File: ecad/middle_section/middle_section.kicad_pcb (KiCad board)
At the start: 2 copper layers, 100 x 80 mm, 28 parts, among them J1 JST SH, J2 JST SH, J5 Conn_01x08, U1 ATtiny1617-M

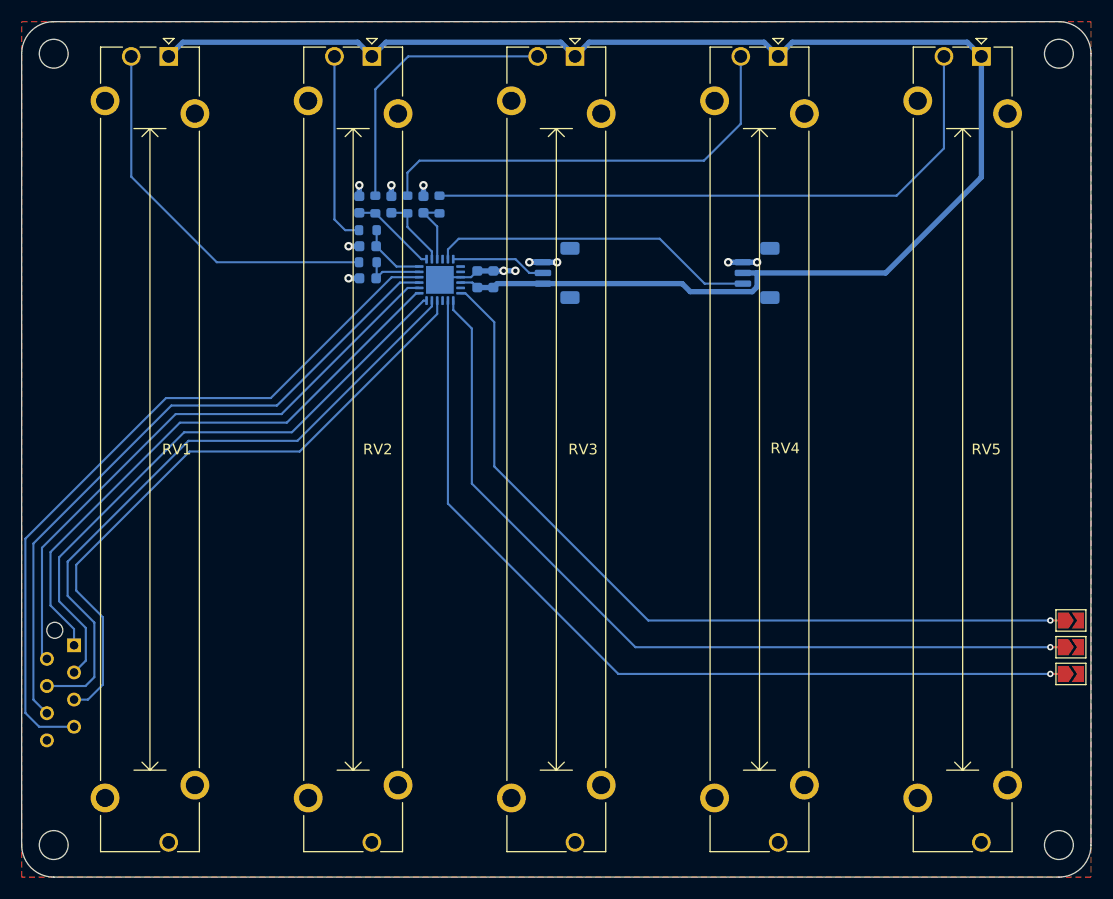
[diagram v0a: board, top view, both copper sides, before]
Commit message: Uses LED Matrix controller on all board.
It simplifies so much the design for a small cost.
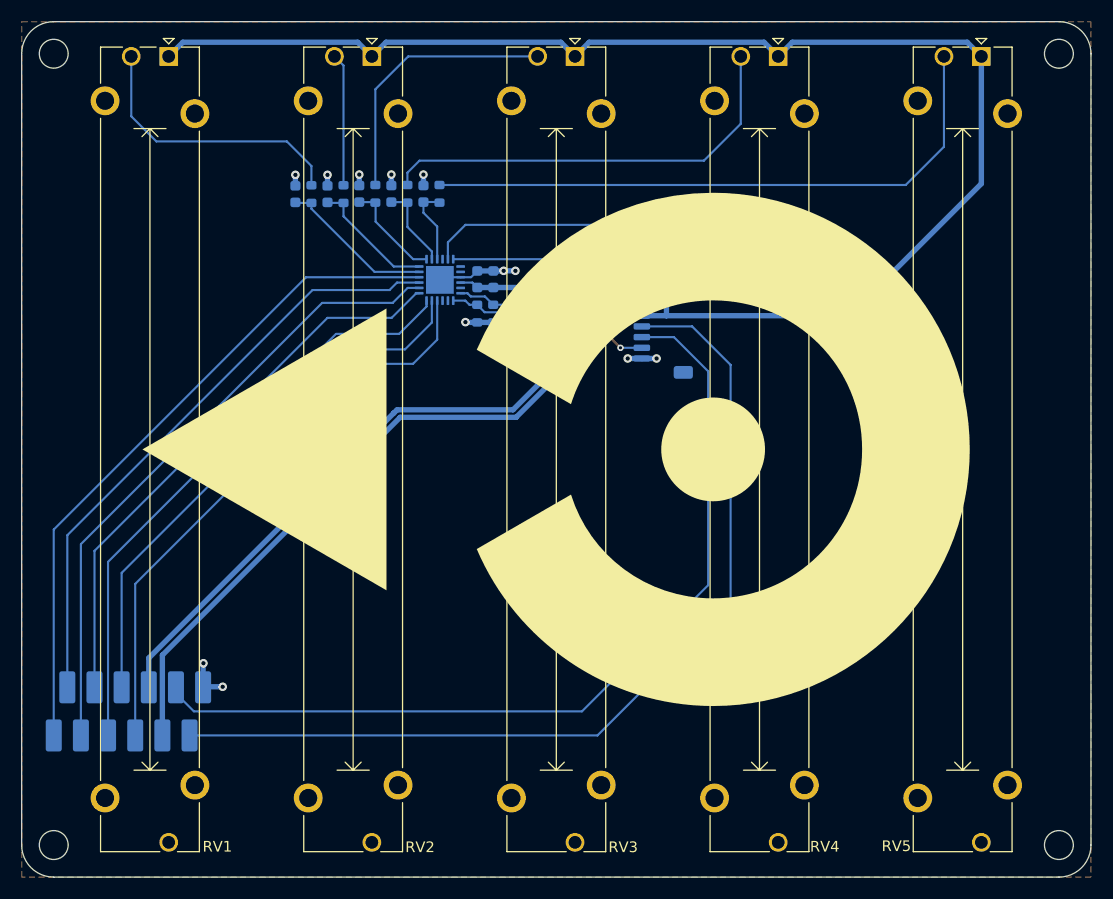
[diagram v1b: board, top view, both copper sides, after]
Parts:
- removed J5: Conn_01x08, Connector_TE-Connectivity:TE_Micro-MaTch_215079-8_2x04_P1.27mm_Vertical
- removed JP3: SolderJumper_2_Open, Jumper:SolderJumper-2_P1.3mm_Open_TrianglePad1.0x1.5mm
- added J3: Micro-MaTch 2x06, woodpecker:TE_Micro-MaTch_1-188275-2_2x06_P1.27mm_Vertical, B.Cu at (98.0, 124.5)
- added R6: 10k, Resistor_SMD:R_0603_1608Metric, B.Cu at (132.1, 87.3)
- added R7: 10k, Resistor_SMD:R_0603_1608Metric, B.Cu at (130.6, 87.3)
- added REF**: OSHW-Logo_11.4x12mm_SilkScreen, Symbol:OSHW-Logo_11.4x12mm_SilkScreen, B.Cu at (151.7, 120.9)
- added kibuzzard-68CC214D: G***, kibuzzard-68CC214D, B.Cu at (139.6, 87.6)
- added kibuzzard-68CC21B9: G***, kibuzzard-68CC21B9, B.Cu at (138.2, 84.3)
- added kibuzzard-68CC21E1: G***, kibuzzard-68CC21E1, B.Cu at (143.1, 90.2)
- added kibuzzard-68CC21F8: G***, kibuzzard-68CC21F8, B.Cu at (143.1, 80.0)
- added kibuzzard-68CC259B: G***, kibuzzard-68CC259B, B.Cu at (176.4, 77.0)
- added kibuzzard-68CC26E5: G***, kibuzzard-68CC26E5, B.Cu at (134.1, 87.6)
- J1: footprint woodpecker:JST_SH_BM03B-SRSS-TB_1x03-1MP_P1.00mm_Vertical -> woodpecker:JST_SH_SM03B-SRSS-TB_1x03-1MP_P1.00mm_Horizontal
- J2: value JST SH -> JST SH 6P; footprint woodpecker:JST_SH_BM03B-SRSS-TB_1x03-1MP_P1.00mm_Vertical -> Connector_JST:JST_SH_SM06B-SRSS-TB_1x06-1MP_P1.00mm_Horizontal
- JP1, JP2: moved to B.Cu
- moved JP2 59.0 mm to (136.7, 86.3), turned to 180 degrees
- moved JP1 56.4 mm to (136.7, 88.9), turned to 180 degrees
- moved J2 11.3 mm to (148.0, 89.0), turned to -90 degrees
- moved C1 10.4 mm to (113.6, 76.1), turned to 90 degrees
- moved J1 9.45 mm to (148.0, 80.0), turned to -90 degrees
- moved R1 8.27 mm to (115.1, 76.1), turned to -90 degrees
- moved C2 6.17 mm to (116.6, 76.1), turned to 90 degrees
- moved R2 4.07 mm to (118.1, 76.1), turned to -90 degrees
- moved C5 1.00 mm to (119.6, 76.1)
- moved C6 1.00 mm to (122.6, 76.1)
- moved C7 1.00 mm to (125.6, 76.1)
- moved R3 1.00 mm to (121.1, 76.1)
- moved R4 1.00 mm to (124.1, 76.1)
- moved R5 1.00 mm to (127.1, 76.1)
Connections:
- J2 pad 1: +3V3 -> +5V
- J2 pad 2: /TX -> +3V3
- J2 pad 3: GND -> /SDA
- JP1 pad 2: GND -> +3V3
- JP2 pad 2: GND -> +3V3
- U1 pad 10: /COL5 -> /R5_SW
- U1 pad 11: /COL4 -> /R6_SW
- U1 pad 12: /COL3 -> /COL5
- U1 pad 13: /COL1 -> /COL4
- U1 pad 14: /COL2 -> /COL3
- U1 pad 15: /R6_SW -> /COL2
- U1 pad 16: /R5_SW -> /COL1
- U1 pad 8: /A2 -> unconnected-(U1-PA7-Pad8)
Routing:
- net /SDA: track 0.00 -> 87.7 mm
- net /SCL: track 0.00 -> 83.4 mm
- net /A2: track 83.1 -> 0.00 mm, vias 1 -> 0
- net +3V3: track 147.6 -> 227.5 mm
- net /A0: track 76.9 -> 12.4 mm, vias 1 -> 0
- net +5V: track 0.00 -> 62.5 mm
- net /A1: track 79.5 -> 17.4 mm, vias 1 -> 0
- net /TX: track 8.92 -> 23.7 mm, vias 0 -> 2
- net /R5_SW: track 68.3 -> 55.5 mm
- net /R6_SW: track 62.6 -> 51.5 mm
- net /UDPI: track 30.6 -> 20.4 mm
- net /CH0_RAW: track 35.9 -> 26.2 mm
- net /COL1: track 54.1 -> 63.2 mm
- net /CH0: track 5.79 -> 14.6 mm
- net /COL4: track 61.1 -> 53.1 mm
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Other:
- board text added: "© Copyright 2025 Alexandre Tuleu"

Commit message: First production run for PCB
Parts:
- removed C4: 10u, Capacitor_SMD:C_0603_1608Metric
- J2: footprint Connector_JST:JST_SH_SM06B-SRSS-TB_1x06-1MP_P1.00mm_Horizontal -> woodpecker:JST_SH_SM06B-SRSS-TB_1x06-1MP_P1.00mm_Horizontal
- R6, R7: value 10k -> 33k
